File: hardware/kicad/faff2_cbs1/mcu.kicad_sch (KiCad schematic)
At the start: 50 parts, among them J1001 USB_C_Receptacle_USB2.0_16P, J1002 TSW-105-07-F-D, SW1001 PTS526, U1001 STM32H723VET6, U1002 USB3320C, U1003 SRAM 32Mb, U1004 MIC5365-1.8, Y1001 24MHz

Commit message: review r1: dissolve test_debug into mcu, split the 24 MHz clock, A2 mcu, ui_io flow
Captain's review, three batches, all landing on mcu.kicad_sch so they ship together.

test_debug.kicad_sch is deleted. Its three blocks moved onto the sheet they serve:
H the SWD + USART3 debug header, J the rail probe header, K the GND hooks - all on
mcu, renumbered into the 10xx range (J401->J1003, R401/402->R1013/1014, J402->J1004,
TP401..406->TP1006..1011, #PWR401..414->#PWR1051..1064). The six SWD/USART3 nets were
shared only with mcu, so they are sheet-local labels now and their twelve sheet pins
came off the root. Nine blocks; pages renumber 2..10 and the refdes ranges become a
fixed table with 4xx retired. Standing rule written into AGENTS.md: test coverage
lives on the circuit page it covers, never its own sheet.

The shared 24 MHz reference is gone. The USB3320 gets its own crystal on REFCLK/XO
(Y1002 ECS-240-12-23G-JGN-TR, 27 pF C0G load caps sized from DS Table 4-11) in a new
block C; the STM32 keeps its own oscillator, minus R1004 and the fan-out. A bare
crystal on the STM32 is impossible without an .ioc change (PH1-OSC_OUT unallocated,
REQ-AR-16), so it stays a driven clock - the two domains now share nothing.

mcu is A2 and re-laid, and all 47 hierarchical labels are right-justified so the
names align outside the wire instead of running into the pin numbers. Net labels
left alone.

ui_io is graphical only, netlist byte-identical: R907 and R915 lie along the signal
(pre-rotated variants in the new faff2_passives.kicad_sym - never an instance
rotation), D903 shunts straight down, and the LIM_A / LIM_B exits are clear of the
+3V3 riser that ran through the LIM_A label.

Verified: ERC 0 errors / 0 warnings at --severity-all, nothing suppressed; netlist
equivalent net-for-net apart from the four rows of the authorised clock change;
411 components, 253 nets, all footprints resolving; overlap checker clean on every
sheet this branch touched. Review PDF deliberately not regene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
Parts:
- removed R1004: 33R, Amodo:R_0603_1608Metric, symbol Amodo_Resistors:RES_TF_33R_0603
- added C1025, C1026: 27pF 2%, Amodo:C_0603_1608Metric, symbol Amodo_Capacitors:CAP_MLCC_27pF_0603_2%_50V_C0G_1
- added J1003: TSW-105-07-F-D, Amodo:TSW-105-07-F-D, symbol Amodo_Connectors:Header_Male_10-way_2-row_Straight_2.54mm_THT
- added J1004: PH1-06-UA, Amodo:Adam_Tech_PH1-06-UA, symbol Amodo_Connectors:Header_Male_6-way_1-row_Straight_2.54mm_THT
- added R1013, R1014: 100R, Amodo:R_0603_1608Metric, symbol Amodo_Resistors:RES_TF_100R_0603
- added TP1006, TP1007, TP1008, TP1009, TP1010, TP1011: TestPoint, Amodo:KeystoneMiniatureTestLoop, symbol Amodo_Connectors:TestPointHook
- added Y1002: 24MHz 18pF, Amodo:Crystal_SMD_0603_2Pin_6.0x3.5mm, symbol Amodo_Crystals:ECS-240-12-23G-JGN-TR_1
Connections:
- net +3V3: now also J1003.1 (Pin_1), J1004.2
- net +3V3A: now also J1004.3
- net DBG_RX: now also R1013.2
- net DBG_TX: now also R1014.2
- net GND: now also C1025.2, C1026.2, J1003.3 (Pin_3), J1003.5 (Pin_5), J1003.9 (Pin_9), J1004.4, J1004.5, J1004.6, TP1006.1, TP1007.1, TP1008.1, TP1009.1, TP1010.1, TP1011.1
- net MCU_nRESET: now also J1003.10 (Pin_10)
- net SWCLK: now also J1003.4 (Pin_4)
- net SWDIO: now also J1003.2 (Pin_2)
- net SWO: now also J1003.6 (Pin_6)
- net USB_REFCLK_24M: now also C1025.1, Y1002.1
- net USB_XO_24M: now reaches U1002.25 (XO)
- net USB_XO_24M: now also C1026.1, Y1002.2
- new net: J1003.7 (Pin_7), R1013.1
- new net: J1003.8 (Pin_8), R1014.1
- new net +5V: J1004.1
- no-connect marks 11 -> 10
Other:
- note added: "24 MHz LVCMOS MEMS oscillator, 10 ppm, driving the STM32 HSE ONLY - the USB3320 now has its own crystal (block C), so the two clock domains share nothing. STM32 HSE is an EXTERNAL CLOCK on PH0 (PH1-OSC_OUT unallocated in the .ioc, REQ-AR-16), so no bare crystal here. 33R source-terminates the one trace."
- note added: "B STM32 24 MHz HSE OSCILLATOR"
- note added: "C USB3320 24 MHz CRYSTAL (ITS OWN REFERENCE)"
- note added: "H SWD + USART3 DEBUG HEADER (REQ-AR-15)"
- note added: "J RAIL PROBE HEADER (TEST_PLAN 4)"
- note added: "K GND HOOKS FOR SCOPE CLIPS"
- note added: "One header to check every logic rail with a DMM during bring-up steps 2 and 3 of TEST_PLAN 5. The rails themselves, and their isolation links and current breaks, belong to power_rails - this header only observes them. 1 +5V 2 +3V3 3 +3V3A 4 GND 5 GND 6 GND +24V IS DELIBERATELY NOT ON THIS HEADER. 24 V next to 3.3 V on a 2.54 mm strip is one slip away from destroying the board; power_entry_24v alr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"
- note added: "PINOUT - standard ARM Cortex Debug 10-pin order on 2.54 mm pitch, so a 2x5 SWD probe cable plugs straight on: 1 VTref (+3V3) 2 SWDIO 3 GND 4 SWCLK 5 GND 6 SWO 7 DBG_RX 8 DBG_TX 9 GND 10 nRESET Pins 7 and 8 are KEY / NC on the ARM pinout and are reused here for the USART3 console (REQ-AR-15 and the block diagram both put SWD and UART on ONE header). They are SWD-safe: an SWD probe drives only 2, 4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"
- note added: "STM32H723VET6 + USB3320 ULPI PHY + USB-C (data only) + OCTOSPI1 PSRAM, with the board's debug and bring-up access alongside it (blocks H, J, K). Pin map authority: hardware/cubemx/ARIA_SRB_FAFF_2_POC_CBs_1.ioc (DEC-0013) - nothing here re-pins it. Local labels stay on this sheet: ULPI_*, QSPI_P1_*, USB_*, HSE_CLK_24M, USB_REFCLK_24M, USB_XO_24M, USB3320_nRESET, SPARE_*, +3V3_USB, +1V8_USB - and n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"
- note added: "Six through-hole GND loops, spread across the board at layout so an oscilloscope ground clip is never far from the signal hook being probed. The house standard asks for these wherever TestPointHook is used, and the block sheets use hooks on I2C1, SPI2, SPI3 and the fault lines."
- note added: "TEST ACCESS (TEST_PLAN 4). The whole test_debug sheet lives here now: block H is the SWD + USART3 debug header, J the rail probe header, K the GND hooks. Test coverage belongs on the page it covers, not on a sheet of its own - docs/decisions/actuator-rev-testdebug.md. Other TPs: NRST (hook), BOOT0, HSE clock (dual TP, block B), +3V3_USB and +1V8_USB (block E). MCO2 leaves the sheet as ADS1235_CLK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"
- note added: "The USB3320 has its own 24 MHz reference: an ECS-240-12-23G-JGN-TR crystal on the PHY's internal oscillator between REFCLK and XO (DS Figure 5-4). It shares nothing with the STM32 HSE oscillator in block B. REFSEL[2:0] = 111 still selects a 24 MHz reference (DS Table 5-10), so no configuration changes. Crystal: fundamental, parallel resonant, CL 18 pF, -40 to +85 C. DS Table 4-11 asks for CL 20 p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"
- note added: "USB3320C-EZK-TR, ULPI OUTPUT CLOCK mode: the PHY generates the 60 MHz ULPI clock on CLKOUT -> STM32 ULPI_CK (PA5). Its 24 MHz reference is its OWN crystal on REFCLK / XO (block C) - no clock is shared with the STM32. REFSEL[2:0]=111 still selects 24 MHz (DS Table 5-10). RBIAS 8.06k 1% and RVBUS 10k (device-only) are datasheet-mandated values (DS 2.1, Table 5-7). ID tied to VDD33 = device-only ope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"
- note removed: "24 MHz LVCMOS MEMS oscillator, 10 ppm (USB needs +/-500 ppm). STM32 HSE is an EXTERNAL CLOCK on PH0 only - PH1-OSC_OUT is unallocated in the .ioc, so a bare crystal is not possible (REQ-AR-16). USB3320 REFSEL[2:0] = 111 selects a 24 MHz reference (DS Table 5-10). 33R per branch source-terminates the two-load fan-out. Resolves OQ-03."
- note removed: "B 24 MHz REFERENCE (STM32 HSE + USB3320 REFCLK)"
- note removed: "STM32H723VET6 + USB3320 ULPI PHY + USB-C (data only) + OCTOSPI1 PSRAM Pin map authority: hardware/cubemx/ARIA_SRB_FAFF_2_POC_CBs_1.ioc (DEC-0013) - nothing here re-pins it. Local labels stay on this sheet: ULPI_*, QSPI_P1_*, USB_*, HSE_CLK_24M, USB3320_nRESET, SPARE_*, +3V3_USB, +1V8_USB. Hierarchical labels leave it; the full list, and the naming choices behind it, are in docs/decisions/actuator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"
- note removed: "TEST ACCESS (TEST_PLAN 4). TPs: NRST (hook), BOOT0, HSE clock (dual TP at the oscillator, block B), +3V3_USB and +1V8_USB (block E). MCO2 leaves the sheet as ADS1235_CLKIN and is probed in loadcell_afe, which owns that net's break. Supply-pin groups are reachable at the decoupling banks in blocks A, D, E and F. DELIBERATELY NO test points on ULPI or OCTOSPI (DEC-0018 ruling 1 / TEST_PLAN 2.2). RO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"
- note removed: "USB3320C-EZK-TR, ULPI OUTPUT CLOCK mode: the PHY generates the 60 MHz ULPI clock on CLKOUT -> STM32 ULPI_CK (PA5). REFCLK takes the shared 24 MHz reference; REFSEL[2:0]=111 (DS Table 5-10). RBIAS 8.06k 1% and RVBUS 10k (device-only) are datasheet-mandated values (DS 2.1, Table 5-7). ID tied to VDD33 = device-only operation (DS 5.6.1). CPEN / SPK_L / SPK_R / XO / N-C are unused: no OTG VBUS switch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"
- moved on the sheet: J1002, U1001B, U1001C, U1001D, U1001E, U1001F

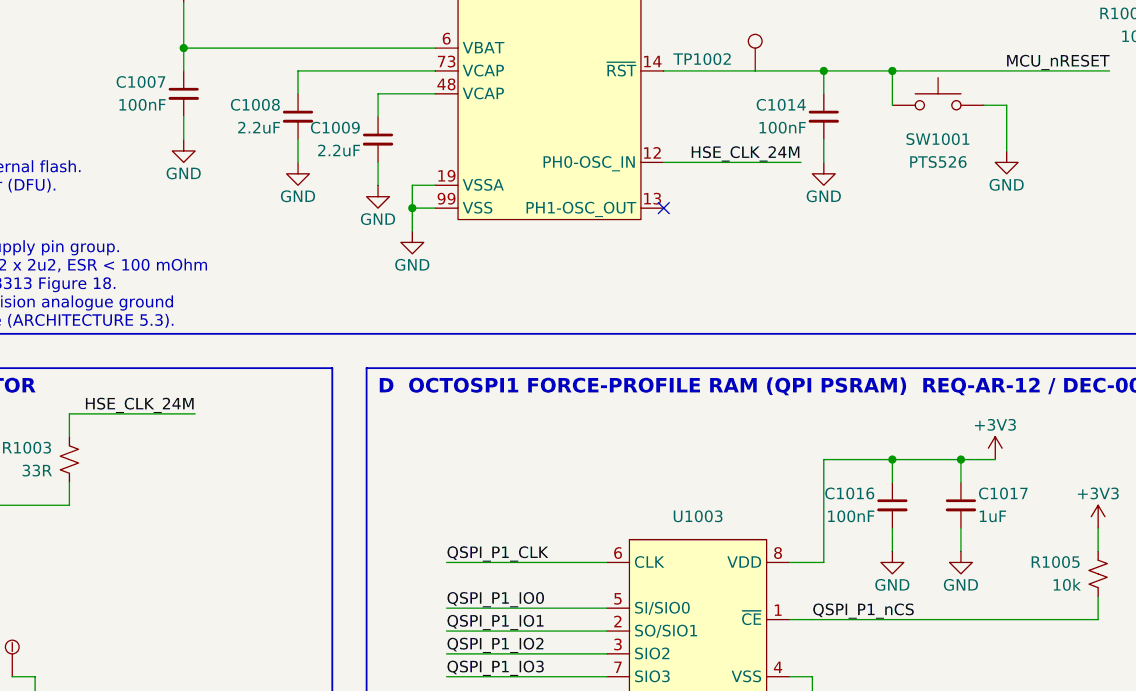
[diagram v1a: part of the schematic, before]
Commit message: review r1 final sweep: power labels, TP silkscreen names, text overlaps
The captain's design-wide pass, run once the per-sheet batches had landed.
Presentation only: ERC 0 errors / 0 warnings at severity-all, 404 components,
251 nets, and every per-net node set identical to the pre-sweep export.

  power labels   92 rail names were hidden on loadcell_afe, motor_drive and
                 temp_sense - all 285 power symbols now read, placed to the
                 house pattern (GND below the symbol, rail arrows above)
  test points    66 of 83 still carried the library default "TestPoint". All
                 83 now name what they measure, from the net they actually
                 land on in the netlist; longest is 5 characters
  text overlap   16 collisions cleared design-wide, four of them sub-millimetre
                 ones the bundled checker passes because it under-measures text
  GND upside down  none - 0 of 285 power symbols is rotated or mirrored
  graphic/wire   one: power_rails block D's bottom border lay along the last
                 PWR_FLAG's wire; the flag column moved up 2.54

The overlap checker turns out to have three separable blind spots, each settled
here by measuring a render rather than by reading the format: it grows every
text field rightward regardless of justify/mirror/180-rotation, so its box is a
mirror image of the truth for those and it both invents and misses collisions;
it measures text at ~1.06 mm per character where the real advance is ~1.19; and
it reflects a rotated symbol's body about the origin. tools/sch_geom.py models
all three correctly and the design is clean under it design-wide. Two of that
model's own rules - notes growing up from their anchor, and labels taking no
180-degree justify flip - were bugs of mine that the checker caught first. The
render is what settles it; neither tool is authoritative alone.

Placement is searched rather than guessed: 177 newly visible fields are tried
against every wire, block border, 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
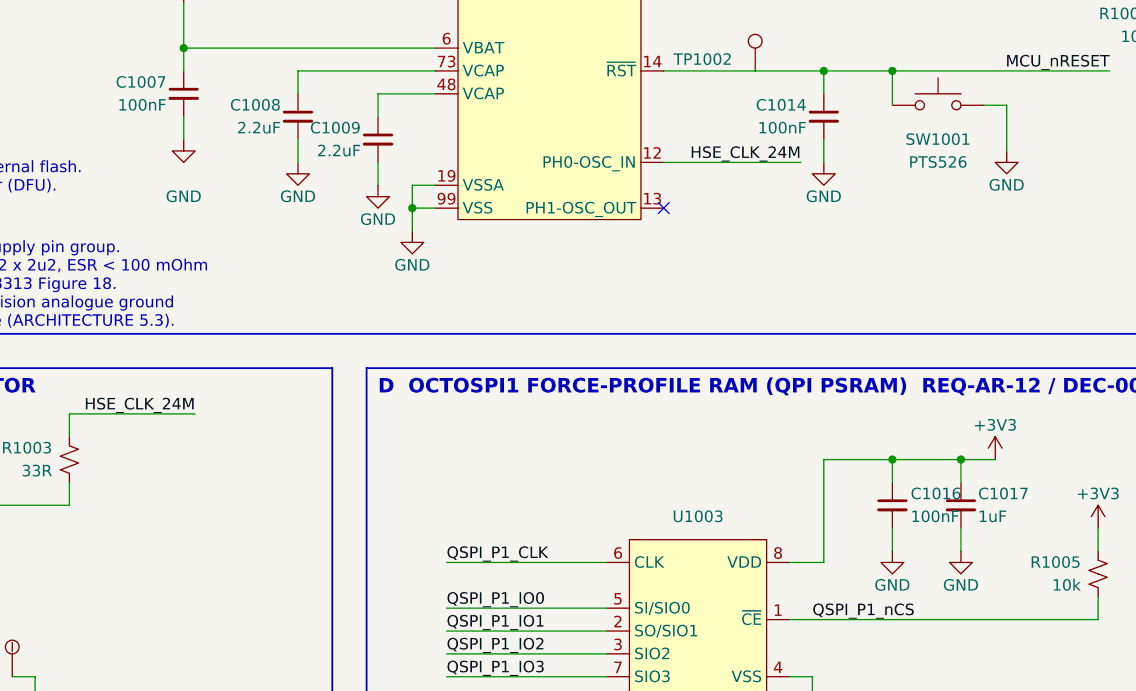
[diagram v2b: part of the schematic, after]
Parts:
- TP1001: value TestPoint -> BOOT0
- TP1002: value TestPoint -> nRST
- TP1003: value TestPoint -> 24MHZ
- TP1004: value TestPoint -> 3V3U
- TP1005: value TestPoint -> 1V8U
- TP1006, TP1007, TP1008, TP1009, TP1010, TP1011: value TestPoint -> GND
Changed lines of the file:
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@@
 		)
 		(property "Value" "GND"
-			(at 83.82 60.96 0)
+			(at 83.82 63.5 0)
 			(effects (font (size 1.27 1.27)))
 		)
@@
 			(effects (font (size 1.27 1.27)) (justify right))
 		)
-		(property "Value" "TestPoint"
-			(at 175.26 45.72 0)
+		(property "Value" "BOOT0"
+			(at 172.72 40.5 0)
 			(effects (font (size 1.27 1.27)) (justify right) (hide yes))
 		)
@@
 			(effects (font (size 1.27 1.27)) (justify right))
 		)
-		(property "Value" "TestPoint"
-			(at 147.32 55.88 0)
+		(property "Value" "nRST"
+			(at 144.78 50.66 0)
 			(effects (font (size 1.27 1.27)) (justify right) (hide yes))
 		)
@@
 			(effects (font (size 1.27 1.27)) (justify right))
 		)
-		(property "Value" "TestPoint"
-			(at 63.5 123.19 0)
+		(property "Value" "24MHZ"
+			(at 59.69 117.97 0)
 			(effects (font (size 1.27 1.27)) (justify right) (hide yes))
 		)
@@
 		(dnp no)
 		(property "Reference" "C1016"
-			(at 160.655 96.52 0)
-			(effects (font (size 1.27 1.27)) (justify right))
+			(at 164.59 96.52 0)
+			(effects (font (size 1.27 1.27)) (justify left))
 		)
 		(property "Value" "100nF"
-			(at 160.655 99.06 0)
-			(effects (font (size 1.27 1.27)) (justify right))
+			(at 164.59 99.06 0)
+			(effects (font (size 1.27 1.27)) (justify left))
 		)
 		(property "Footprint" "Amodo:C_0402_1005Metric"
@@
 			(effects (font (size 1.27 1.27)))
 		)
-		(property "Value" "TestPoint"
-			(at 318.77 110.49 0)
+		(property "Value" "3V3U"
+			(at 316.23 102.73 0)
 			(effects (font (size 1.27 1.27)) (hide yes))
 		)
@@
 			(effects (font (size 1.27 1.27)) (justify left))
 		)
-		(property "Value" "TestPoint"
-			(at 351.79 118.11 0)
+		(property "Value" "1V8U"
+			(at 354.33 112.89 0)
 			(effects (font (size 1.27 1.27)) (justify left) (hide yes))
 		)
@@
 			(effects (font (size 1.27 1.27)) (justify right))
 		)
-		(property "Value" "TestPoint"
-			(at 166.37 308.61 0)
+		(property "Value" "GND"
+			(at 163.83 303.39 0)
 			(effects (font (size 1.27 1.27)) (justify right) (hide yes))
 		)
@@
 			(effects (font (size 1.27 1.27)) (justify right))
 		)
-		(property "Value" "TestPoint"
-			(at 191.77 308.61 0)
+		(property "Value" "GND"
+			(at 189.23 303.39 0)
 			(effects (font (size 1.27 1.27)) (justify right) (hide yes))
 		)
@@
 			(effects (font (size 1.27 1.27)) (justify right))
 		)
-		(property "Value" "TestPoint"
-			(at 217.17 308.61 0)
+		(property "Value" "GND"
+			(at 214.63 303.39 0)
 			(effects (font (size 1.27 1.27)) (justify right) (hide yes))
 		)
@@
 			(effects (font (size 1.27 1.27)) (justify right))
 		)
-		(property "Value" "TestPoint"
-			(at 242.57 308.61 0)
+		(property "Value" "GND"
+			(at 240.03 303.39 0)
 			(effects (font (size 1.27 1.27)) (justify right) (hide yes))
 		)
@@
 			(effects (font (size 1.27 1.27)) (justify right))
 		)
-		(property "Value" "TestPoint"
-			(at 267.97 308.61 0)
+		(property "Value" "GND"
+			(at 265.43 303.39 0)
 			(effects (font (size 1.27 1.27)) (justify right) (hide yes))
 		)
@@
 			(effects (font (size 1.27 1.27)) (justify right))
 		)
-		(property "Value" "TestPoint"
-			(at 293.37 308.61 0)
+		(property "Value" "GND"
+			(at 290.83 303.39 0)
 			(effects (font (size 1.27 1.27)) (justify right) (hide yes))
 		)

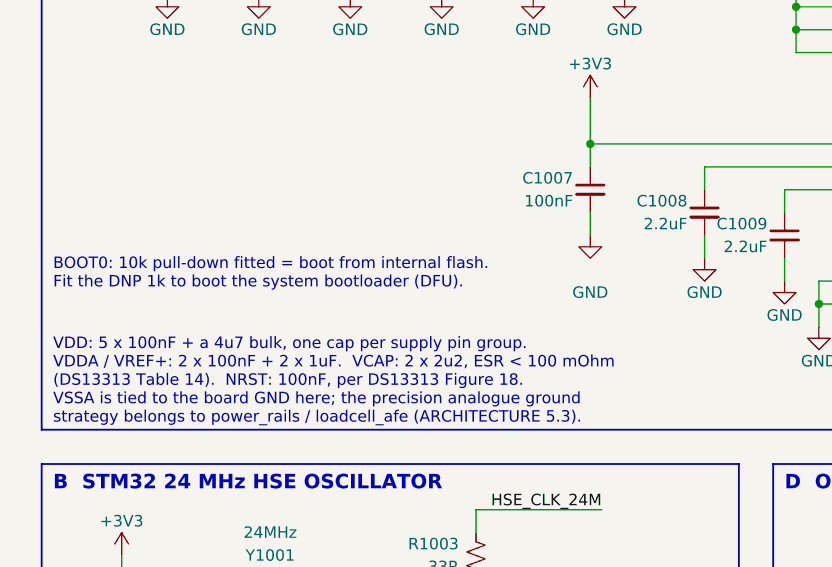
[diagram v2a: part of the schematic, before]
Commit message: review r2 item 8: one placement rule for every power symbol's net name
"Directly above it, centre justified, and close" - applied as no sideways
offset, centred, 3.81 mm away: above a rail arrow, below a ground. All 283
power symbols now carry it; 103 did not, most left-anchored rather than centred
and a few offset up to 7.6 mm sideways by round 1's auto-placer.

The ground mirror is an interpretation and is flagged as such: "above" a GND
symbol is where its wire arrives, and 137 instances plus every convention put
GND's name under the triangle. One line to change if the captain meant it
literally.

What makes this different from round 1 is that the label is now PINNED, so
everything else moves instead - the symbol along its own stub, a note to the
nearest clear spot, a block box outward (five rectangles grew where a name sat
on a border with clear space beyond), and two PWR_FLAGs placed by hand because
their 9.5 mm names do not fit the 10 mm rail runs they tap.

Thirteen of 283 still graze a wire, body or note on the two densest sheets and
are listed in the decisions file rather than hidden. Each needs the parts around
it respaced, which is more than a label sweep should do unasked - the TIM1 note
on motor_drive in particular has nowhere to go: no clear position exists for a
47.6 x 8.7 mm box anywhere in that block.

Also recorded: my own severity metric scored wire-through-text at zero for a
while, because a wire is a zero-thickness segment and box-intersection depth
against it is always 0. For those, severity is how far inside the box the line
sits. A render caught it; the number did not.

ERC 0 errors / 0 warnings at severity-all; 412 components, 259 nets, node sets
identical to before the batch. Review PDF regenerated once, here, for the whole
of round 2.

Co-Authored-By: Claude Opus 5 <noreply@anthropic.com>
Claude-Session: https://claude.ai/code/session_01PFWfwT8RZc8Zqn8vgZxV8j
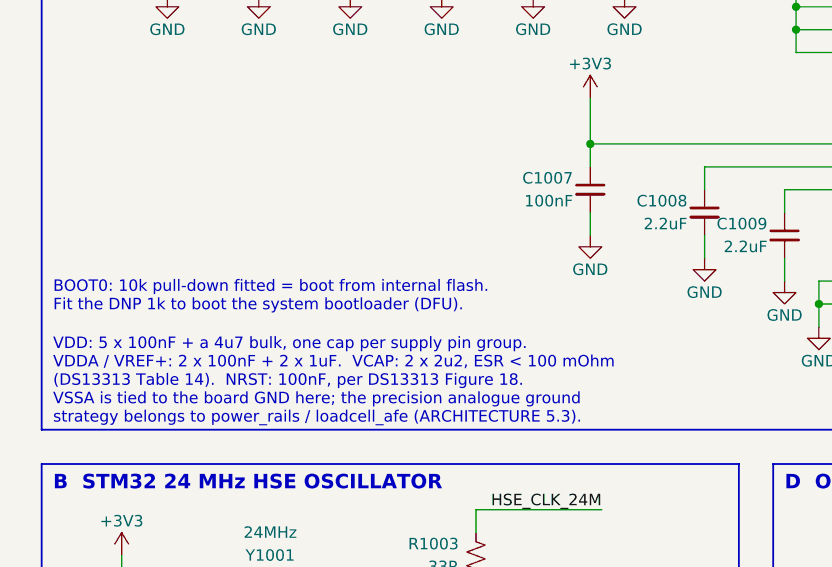
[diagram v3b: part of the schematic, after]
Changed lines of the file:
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@@
 		)
 		(property "Value" "GND"
-			(at 83.82 63.5 0)
+			(at 83.82 60.96 0)
 			(effects (font (size 1.27 1.27)))
 		)
@@
 	(text "BOOT0: 10k pull-down fitted = boot from internal flash.\nFit the DNP 1k to boot the system bootloader (DFU)."
 		(exclude_from_sim no)
-		(at 24.13 59.69 0)
+		(at 24.13 62.23 0)
 		(effects (font (size 1.27 1.27)) (justify left top))
 	)
